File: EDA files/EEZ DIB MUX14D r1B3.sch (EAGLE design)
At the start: 66 parts, among them IC1 STM32F030C6T6, IC2 74HC1G126GW,125, IC3 M24C32-WMN6P, IC4 LP2985-33DBVR, IC5 TLV9001IDBVR, IC6 LM335, IC7 ULN2803ADWR, IC8 ULN2803ADWR, K1 3572.1220.051, K10 3572.1220.051, K11 3572.1220.051, K12 3572.1220.051, K13 3572.1220.051, K14 3572.1220.051, K15 3572.1220.051, K16 3572.1220.051, K17 3572.1220.051, K2 3572.1220.051, K3 3572.1220.051, K4 3572.1220.051, K5 3572.1220.051, K6 3572.1220.051, K7 3572.1220.051, K8 3572.1220.051, K9 3572.1220.051, Q1 2N7002, X1 N.C., X2 77317-104-28LF, X3 DS1014-10RF1B, X4 DS1014-10RF1B, X5 691327310016, X6 691327310016

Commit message: Centroid files
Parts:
- removed C8: ???, rcl:C-EUC0805
- removed R2: ???, rcl:R-EU_R0805
- IC5: value TLV9001IDBVR -> MCP6001RT-I/OT
- R4, R5: value 30K -> 10K
- R6: value 120K -> 40K2
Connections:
- removed net N$6: IC1.PA7, R2.1
- net CJ_AIN: now also IC1.PA7; no longer C8.2, R2.2
- net GND: no longer C8.1
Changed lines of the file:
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@@
 <part name="R3" library="rcl" deviceset="R-EU_" device="R0805" value="1K5"/>
 <part name="SUPPLY18" library="supply2" deviceset="GND" device=""/>
-<part name="R2" library="rcl" deviceset="R-EU_" device="R0805" value="???"/>
-<part name="C8" library="rcl" deviceset="C-EU" device="C0805" value="???"/>
-<part name="SUPPLY19" library="supply2" deviceset="GND" device=""/>
 <part name="P+7" library="supply1" deviceset="+5V" device=""/>
 <part name="C12" library="rcl" deviceset="C-EU" device="C0603" value="100n"/>
 <part name="SUPPLY20" library="supply2" deviceset="GND" device=""/>
-<part name="IC5" library="EEZ_TI" deviceset="OPA376A" device="IDBVR" value="TLV9001IDBVR"/>
-<part name="R4" library="rcl" deviceset="R-EU_" device="R0805" value="30K"/>
-<part name="R5" library="rcl" deviceset="R-EU_" device="R0805" value="30K"/>
-<part name="R6" library="rcl" deviceset="R-EU_" device="R0805" value="120K"/>
+<part name="IC5" library="EEZ_TI" deviceset="OPA376A" device="IDBVR" value="MCP6001RT-I/OT"/>
+<part name="R4" library="rcl" deviceset="R-EU_" device="R0805" value="10K"/>
+<part name="R5" library="rcl" deviceset="R-EU_" device="R0805" value="10K"/>
+<part name="R6" library="rcl" deviceset="R-EU_" device="R0805" value="40K2"/>
 <part name="+3V1" library="supply1" deviceset="+3V3" device=""/>
 <part name="C14" library="rcl" deviceset="C-EU" device="C0805" value="100p"/>
@@
 <attribute name="NAME" x="102.87" y="72.009" size="1.778" layer="95" rot="R180"/>
 </instance>
-<instance part="R2" gate="G$1" x="193.04" y="53.34" smashed="yes" rot="MR0">
-<attribute name="NAME" x="191.77" y="54.8386" size="1.778" layer="95"/>
-<attribute name="VALUE" x="190.5" y="50.038" size="1.778" layer="96"/>
-</instance>
-<instance part="C8" gate="G$1" x="185.42" y="45.72" smashed="yes" rot="R180">
-<attribute name="NAME" x="187.579" y="47.371" size="1.778" layer="95"/>
-<attribute name="VALUE" x="187.579" y="45.466" size="1.778" layer="96"/>
-</instance>
-<instance part="SUPPLY19" gate="GND" x="185.42" y="38.1" smashed="yes">
-<attribute name="VALUE" x="187.325" y="38.735" size="1.778" layer="96" rot="MR180"/>
-</instance>
 </instances>
 <busses>
@@
 <junction x="160.02" y="101.6"/>
 </segment>
-<segment>
-<pinref part="C8" gate="G$1" pin="1"/>
-<wire x1="185.42" y1="43.18" x2="185.42" y2="40.64" width="0.1524" layer="91"/>
-<pinref part="SUPPLY19" gate="GND" pin="GND"/>
-</segment>
 </net>
 <net name="DIB_A0" class="0">
@@
 </segment>
 </net>
-<net name="N$6" class="0">
-<segment>
+<net name="CJ_AIN" class="0">
+<segment>
+<label x="170.18" y="53.975" size="1.27" layer="102"/>
 <pinref part="IC1" gate="G$1" pin="PA7"/>
 <wire x1="200.66" y1="78.74" x2="200.66" y2="53.34" width="0.1524" layer="91"/>
-<pinref part="R2" gate="G$1" pin="1"/>
-<wire x1="198.12" y1="53.34" x2="200.66" y2="53.34" width="0.1524" layer="91"/>
-</segment>
-</net>
-<net name="CJ_AIN" class="0">
-<segment>
-<pinref part="R2" gate="G$1" pin="2"/>
-<pinref part="C8" gate="G$1" pin="2"/>
-<wire x1="187.96" y1="53.34" x2="185.42" y2="53.34" width="0.1524" layer="91"/>
-<wire x1="185.42" y1="53.34" x2="185.42" y2="50.8" width="0.1524" layer="91"/>
-<wire x1="185.42" y1="53.34" x2="170.18" y2="53.34" width="0.1524" layer="91"/>
-<junction x="185.42" y="53.34"/>
-<label x="170.18" y="53.975" size="1.27" layer="102"/>
+<wire x1="170.18" y1="53.34" x2="200.66" y2="53.34" width="0.1524" layer="91"/>
 </segment>
 </net>
@@
 </sheet>
 <sheet>
+<description>Switches, Cold junction</description>
 <plain>
 <text x="2.54" y="6.35" size="1.27" layer="94">Licensed under the TAPR Open Hardware License (www.tapr.org/OHL)</text>
@@
 </sheet>
 <sheet>
+<description>Relay drivers</description>
 <plain>
 <text x="2.54" y="6.35" size="1.27" layer="94">Licensed under the TAPR Open Hardware License (www.tapr.org/OHL)</text>

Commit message: BOM update
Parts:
- IC5: value MCP6001RT-I/OT -> MCP6001T-I/OT
- IC6: value LM335 -> LM335AZ
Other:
- note added: "P2H"
- note removed: "P2LH"
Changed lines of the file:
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@@
 <part name="SUPPLY17" library="supply2" deviceset="GND" device=""/>
 <part name="R7" library="rcl" deviceset="R-EU_" device="R0805" value="100K"/>
-<part name="IC6" library="EEZ_TI" deviceset="LM335" device="-TO92" value="LM335"/>
+<part name="IC6" library="EEZ_TI" deviceset="LM335" device="-TO92" value="LM335AZ"/>
 <part name="R3" library="rcl" deviceset="R-EU_" device="R0805" value="1K5"/>
 <part name="SUPPLY18" library="supply2" deviceset="GND" device=""/>
@@
 <part name="C12" library="rcl" deviceset="C-EU" device="C0603" value="100n"/>
 <part name="SUPPLY20" library="supply2" deviceset="GND" device=""/>
-<part name="IC5" library="EEZ_TI" deviceset="OPA376A" device="IDBVR" value="MCP6001RT-I/OT"/>
+<part name="IC5" library="EEZ_TI" deviceset="OPA376A" device="IDBVR" value="MCP6001T-I/OT"/>
 <part name="R4" library="rcl" deviceset="R-EU_" device="R0805" value="10K"/>
 <part name="R5" library="rcl" deviceset="R-EU_" device="R0805" value="10K"/>
@@
 <text x="222.25" y="132.08" size="1.4224" layer="101">P2L.6</text>
 <text x="222.25" y="127" size="1.4224" layer="101">P2L.7</text>
-<text x="222.25" y="124.46" size="1.4224" layer="101">P2LH</text>
+<text x="222.25" y="124.46" size="1.4224" layer="101">P2H</text>
 <text x="222.25" y="121.92" size="1.4224" layer="101">P2L</text>
 <text x="209.55" y="130.81" size="1.4224" layer="101" rot="R180">P1H.7</text>

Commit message: #1
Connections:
- net P1 renamed P1.C
- net P2 renamed P2.C
- net P2L.6: now also K153.P; no longer K173.P
- net P2L.7: now also K173.P; no longer K153.P
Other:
- moved on the sheet: K15, K17
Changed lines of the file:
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@@
 </segment>
 </net>
-<net name="P2" class="0">
+<net name="P2.C" class="0">
 <segment>
 <pinref part="IC1" gate="G$1" pin="PB7"/>
@@
 </segment>
 </net>
-<net name="P1" class="0">
+<net name="P1.C" class="0">
 <segment>
 <pinref part="IC1" gate="G$1" pin="PB10"/>
@@
 <attribute name="PART" x="147.32" y="132.08" size="1.778" layer="95"/>
 </instance>
-<instance part="K15" gate="3" x="149.86" y="55.88" smashed="yes" rot="R270">
-<attribute name="PART" x="147.32" y="58.42" size="1.778" layer="95"/>
+<instance part="K15" gate="3" x="149.86" y="63.5" smashed="yes" rot="R270">
+<attribute name="PART" x="147.32" y="66.04" size="1.778" layer="95"/>
 </instance>
 <instance part="K17" gate="2" x="149.86" y="121.92" smashed="yes" rot="R270">
 <attribute name="PART" x="147.32" y="124.46" size="1.778" layer="95"/>
 </instance>
-<instance part="K17" gate="3" x="149.86" y="63.5" smashed="yes" rot="R270">
-<attribute name="PART" x="147.32" y="66.04" size="1.778" layer="95"/>
+<instance part="K17" gate="3" x="149.86" y="55.88" smashed="yes" rot="R270">
+<attribute name="PART" x="147.32" y="58.42" size="1.778" layer="95"/>
 </instance>
 <instance part="K9" gate="2" x="78.74" y="144.78" smashed="yes" rot="R270">
@@
 <pinref part="K2" gate="3" pin="S"/>
 <wire x1="154.94" y1="101.6" x2="160.02" y2="101.6" width="0.1524" layer="91"/>
-<pinref part="K17" gate="3" pin="S"/>
-<wire x1="154.94" y1="63.5" x2="160.02" y2="63.5" width="0.1524" layer="91"/>
+<junction x="160.02" y="71.12"/>
+<wire x1="160.02" y1="48.26" x2="160.02" y2="55.88" width="0.1524" layer="91"/>
+<wire x1="160.02" y1="55.88" x2="160.02" y2="63.5" width="0.1524" layer="91"/>
 <wire x1="160.02" y1="63.5" x2="160.02" y2="71.12" width="0.1524" layer="91"/>
-<junction x="160.02" y="71.12"/>
-<pinref part="K15" gate="3" pin="S"/>
-<wire x1="154.94" y1="55.88" x2="160.02" y2="55.88" width="0.1524" layer="91"/>
-<wire x1="160.02" y1="55.88" x2="160.02" y2="63.5" width="0.1524" layer="91"/>
-<junction x="160.02" y="63.5"/>
 <wire x1="160.02" y1="86.36" x2="175.26" y2="86.36" width="0.1524" layer="91"/>
 <pinref part="X6" gate="-8" pin="1"/>
 <wire x1="132.08" y1="48.26" x2="160.02" y2="48.26" width="0.1524" layer="91"/>
-<wire x1="160.02" y1="48.26" x2="160.02" y2="55.88" width="0.1524" layer="91"/>
-<junction x="160.02" y="55.88"/>
 <label x="134.62" y="48.895" size="1.27" layer="102"/>
 <label x="165.1" y="86.995" size="1.27" layer="102"/>
@@
 <pinref part="K11" gate="3" pin="S"/>
 <label x="96.52" y="107.315" size="1.27" layer="102" rot="MR0"/>
+<pinref part="K15" gate="3" pin="S"/>
+<wire x1="154.94" y1="63.5" x2="160.02" y2="63.5" width="0.1524" layer="91"/>
+<junction x="160.02" y="63.5"/>
+<pinref part="K17" gate="3" pin="S"/>
+<wire x1="154.94" y1="55.88" x2="160.02" y2="55.88" width="0.1524" layer="91"/>
+<junction x="160.02" y="55.88"/>
 </segment>
 </net>
@@
 <segment>
 <pinref part="X6" gate="-4" pin="1"/>
-<pinref part="K17" gate="3" pin="P"/>
 <wire x1="132.08" y1="63.5" x2="144.78" y2="63.5" width="0.1524" layer="91"/>
 <label x="134.62" y="64.135" size="1.27" layer="102"/>
+<pinref part="K15" gate="3" pin="P"/>
 </segment>
 </net>
@@
 <segment>
 <pinref part="X6" gate="-6" pin="1"/>
-<pinref part="K15" gate="3" pin="P"/>
 <wire x1="132.08" y1="55.88" x2="144.78" y2="55.88" width="0.1524" layer="91"/>
 <label x="134.62" y="56.515" size="1.27" layer="102"/>
+<pinref part="K17" gate="3" pin="P"/>
 </segment>
 </net>
@@
 </segment>
 </net>
-<net name="P1" class="0">
+<net name="P1.C" class="0">
 <segment>
 <pinref part="IC7" gate="A" pin="8B"/>
@@
 </segment>
 </net>
-<net name="P2" class="0">
+<net name="P2.C" class="0">
 <segment>
 <pinref part="IC8" gate="A" pin="8B"/>

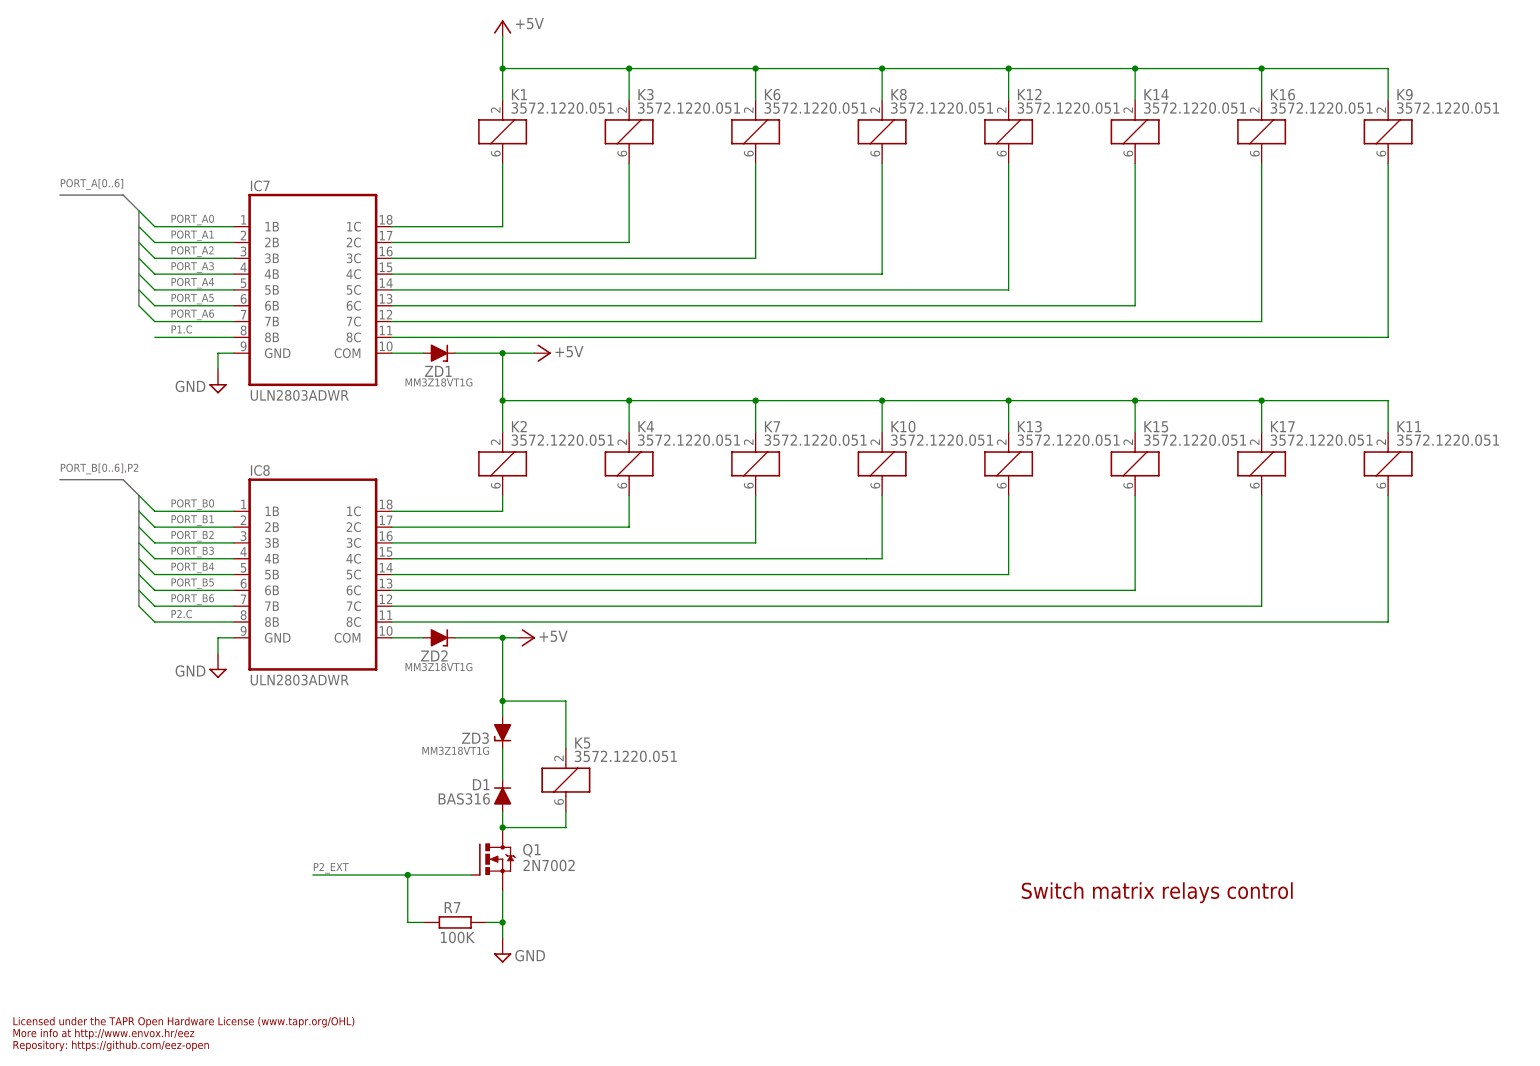
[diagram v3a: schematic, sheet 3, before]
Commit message: Reed relay replacement
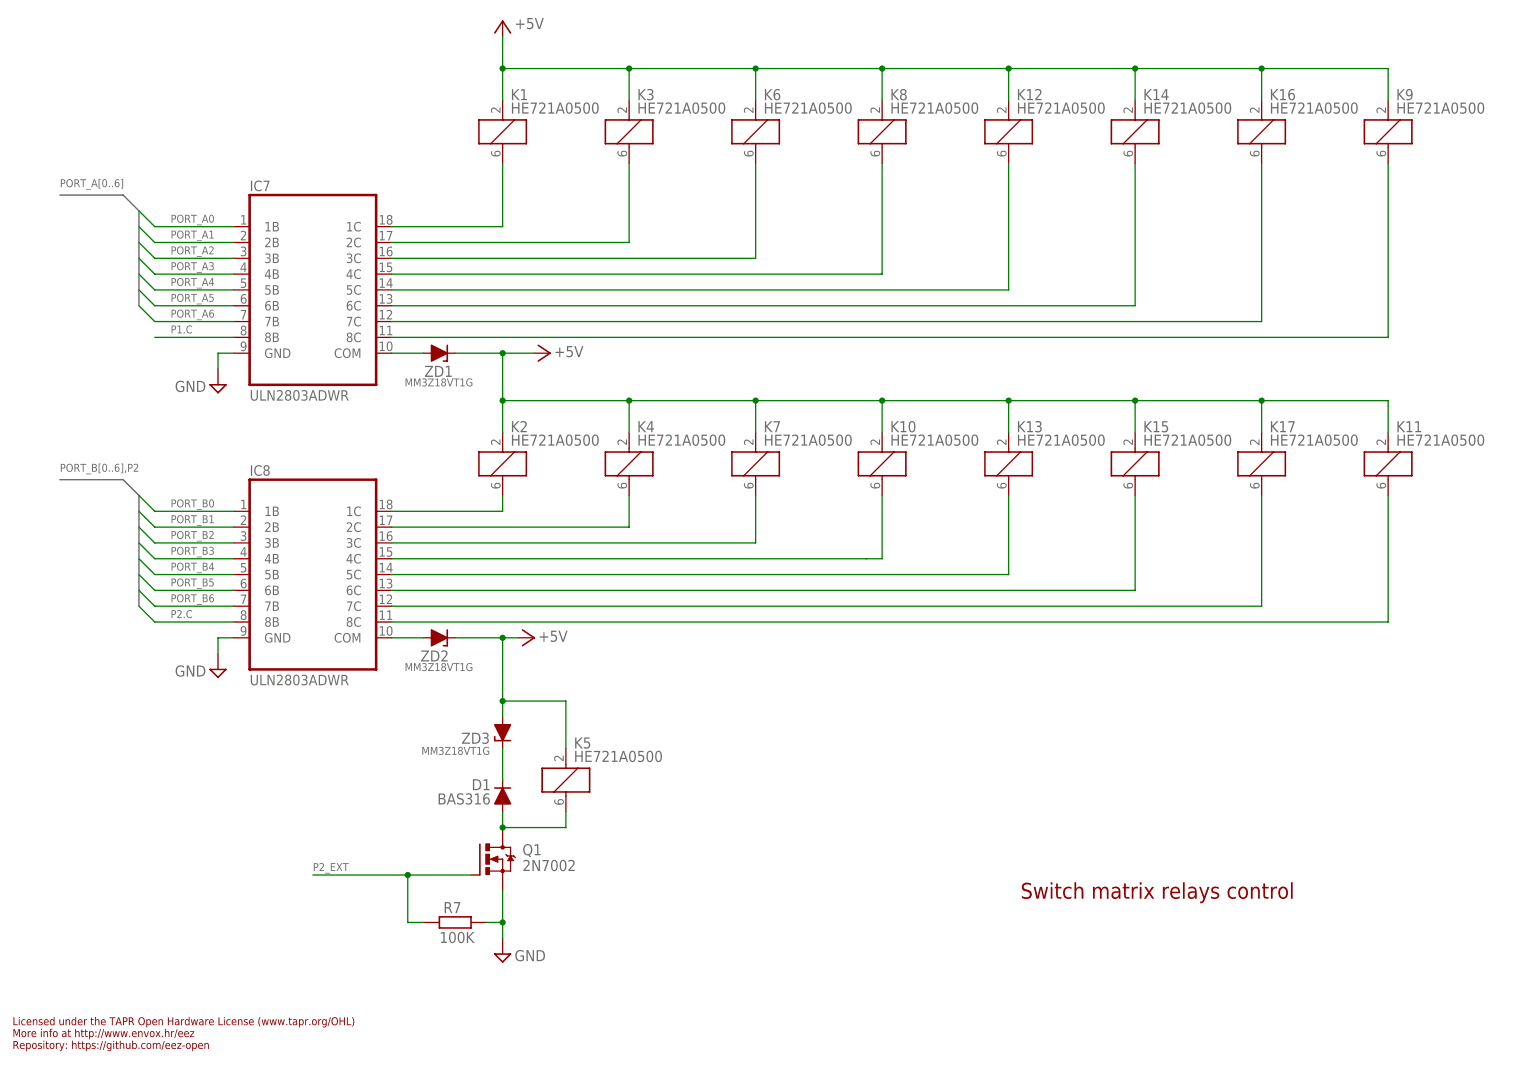
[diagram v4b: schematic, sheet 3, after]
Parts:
- K1, K10, K11, K12, K13, K14, K15, K16, K17, K2, K3, K4, K5, K6, K7, K8, K9: value 3572.1220.051 -> HE721A0500
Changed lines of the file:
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@@
 <part name="X3" library="EEZ_connectors" deviceset="DS1014-10RF1B" device=""/>
 <part name="X4" library="EEZ_connectors" deviceset="DS1014-10RF1B" device=""/>
-<part name="K1" library="EEZ_switches" deviceset="RR2A" device="" value="3572.1220.051"/>
-<part name="K3" library="EEZ_switches" deviceset="RR2A" device="" value="3572.1220.051"/>
-<part name="K6" library="EEZ_switches" deviceset="RR2A" device="" value="3572.1220.051"/>
-<part name="K8" library="EEZ_switches" deviceset="RR2A" device="" value="3572.1220.051"/>
-<part name="K12" library="EEZ_switches" deviceset="RR2A" device="" value="3572.1220.051"/>
-<part name="K14" library="EEZ_switches" deviceset="RR2A" device="" value="3572.1220.051"/>
-<part name="K16" library="EEZ_switches" deviceset="RR2A" device="" value="3572.1220.051"/>
-<part name="K2" library="EEZ_switches" deviceset="RR2A" device="" value="3572.1220.051"/>
-<part name="K4" library="EEZ_switches" deviceset="RR2A" device="" value="3572.1220.051"/>
-<part name="K7" library="EEZ_switches" deviceset="RR2A" device="" value="3572.1220.051"/>
-<part name="K10" library="EEZ_switches" deviceset="RR2A" device="" value="3572.1220.051"/>
-<part name="K13" library="EEZ_switches" deviceset="RR2A" device="" value="3572.1220.051"/>
+<part name="K1" library="EEZ_switches" deviceset="RR2A" device="" value="HE721A0500"/>
+<part name="K3" library="EEZ_switches" deviceset="RR2A" device="" value="HE721A0500"/>
+<part name="K6" library="EEZ_switches" deviceset="RR2A" device="" value="HE721A0500"/>
+<part name="K8" library="EEZ_switches" deviceset="RR2A" device="" value="HE721A0500"/>
+<part name="K12" library="EEZ_switches" deviceset="RR2A" device="" value="HE721A0500"/>
+<part name="K14" library="EEZ_switches" deviceset="RR2A" device="" value="HE721A0500"/>
+<part name="K16" library="EEZ_switches" deviceset="RR2A" device="" value="HE721A0500"/>
+<part name="K2" library="EEZ_switches" deviceset="RR2A" device="" value="HE721A0500"/>
+<part name="K4" library="EEZ_switches" deviceset="RR2A" device="" value="HE721A0500"/>
+<part name="K7" library="EEZ_switches" deviceset="RR2A" device="" value="HE721A0500"/>
+<part name="K10" library="EEZ_switches" deviceset="RR2A" device="" value="HE721A0500"/>
+<part name="K13" library="EEZ_switches" deviceset="RR2A" device="" value="HE721A0500"/>
 <part name="ZD1" library="EEZ_Lib1" deviceset="ZENER-DIODE" device="SOD323R" value="MM3Z18VT1G"/>
 <part name="ZD2" library="EEZ_Lib1" deviceset="ZENER-DIODE" device="SOD323R" value="MM3Z18VT1G"/>
@@
 <part name="P+6" library="supply1" deviceset="+5V" device=""/>
 <part name="P+5" library="supply1" deviceset="+5V" device=""/>
-<part name="K15" library="EEZ_switches" deviceset="RR2A" device="" value="3572.1220.051"/>
-<part name="K17" library="EEZ_switches" deviceset="RR2A" device="" value="3572.1220.051"/>
-<part name="K9" library="EEZ_switches" deviceset="RR2A" device="" value="3572.1220.051"/>
-<part name="K11" library="EEZ_switches" deviceset="RR2A" device="" value="3572.1220.051"/>
-<part name="K5" library="EEZ_switches" deviceset="RR2A" device="" value="3572.1220.051"/>
+<part name="K15" library="EEZ_switches" deviceset="RR2A" device="" value="HE721A0500"/>
+<part name="K17" library="EEZ_switches" deviceset="RR2A" device="" value="HE721A0500"/>
+<part name="K9" library="EEZ_switches" deviceset="RR2A" device="" value="HE721A0500"/>
+<part name="K11" library="EEZ_switches" deviceset="RR2A" device="" value="HE721A0500"/>
+<part name="K5" library="EEZ_switches" deviceset="RR2A" device="" value="HE721A0500"/>
 <part name="P+4" library="supply1" deviceset="+5V" device=""/>
 <part name="D1" library="EEZ_Lib1" deviceset="DIODE" device="SOD323R" value="BAS316"/>
